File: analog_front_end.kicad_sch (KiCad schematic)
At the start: 14 parts

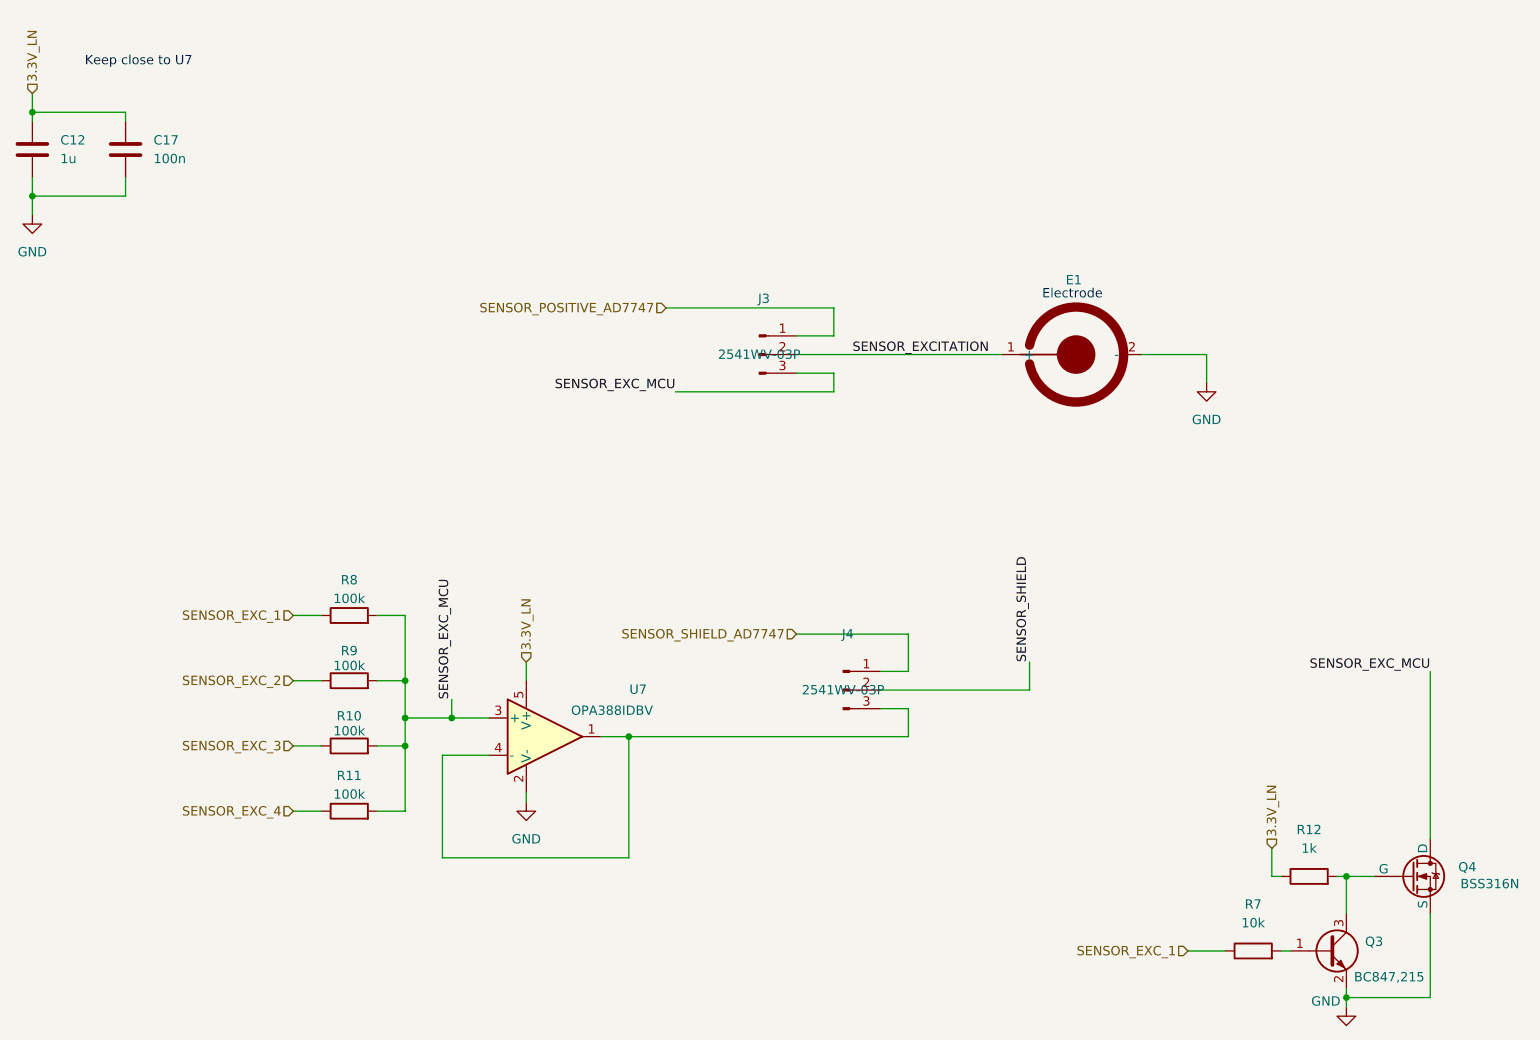
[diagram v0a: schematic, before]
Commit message: bom: Optimize part selection to reduce order price at jlcpcb
- Change references to use basic components instead of 'extended components' when available
- Change button reference to use a basic component
- Change led references to use basic components
- Harmonize some resistors value to limit the number of lines in BoM
- Change transistor references for basic components
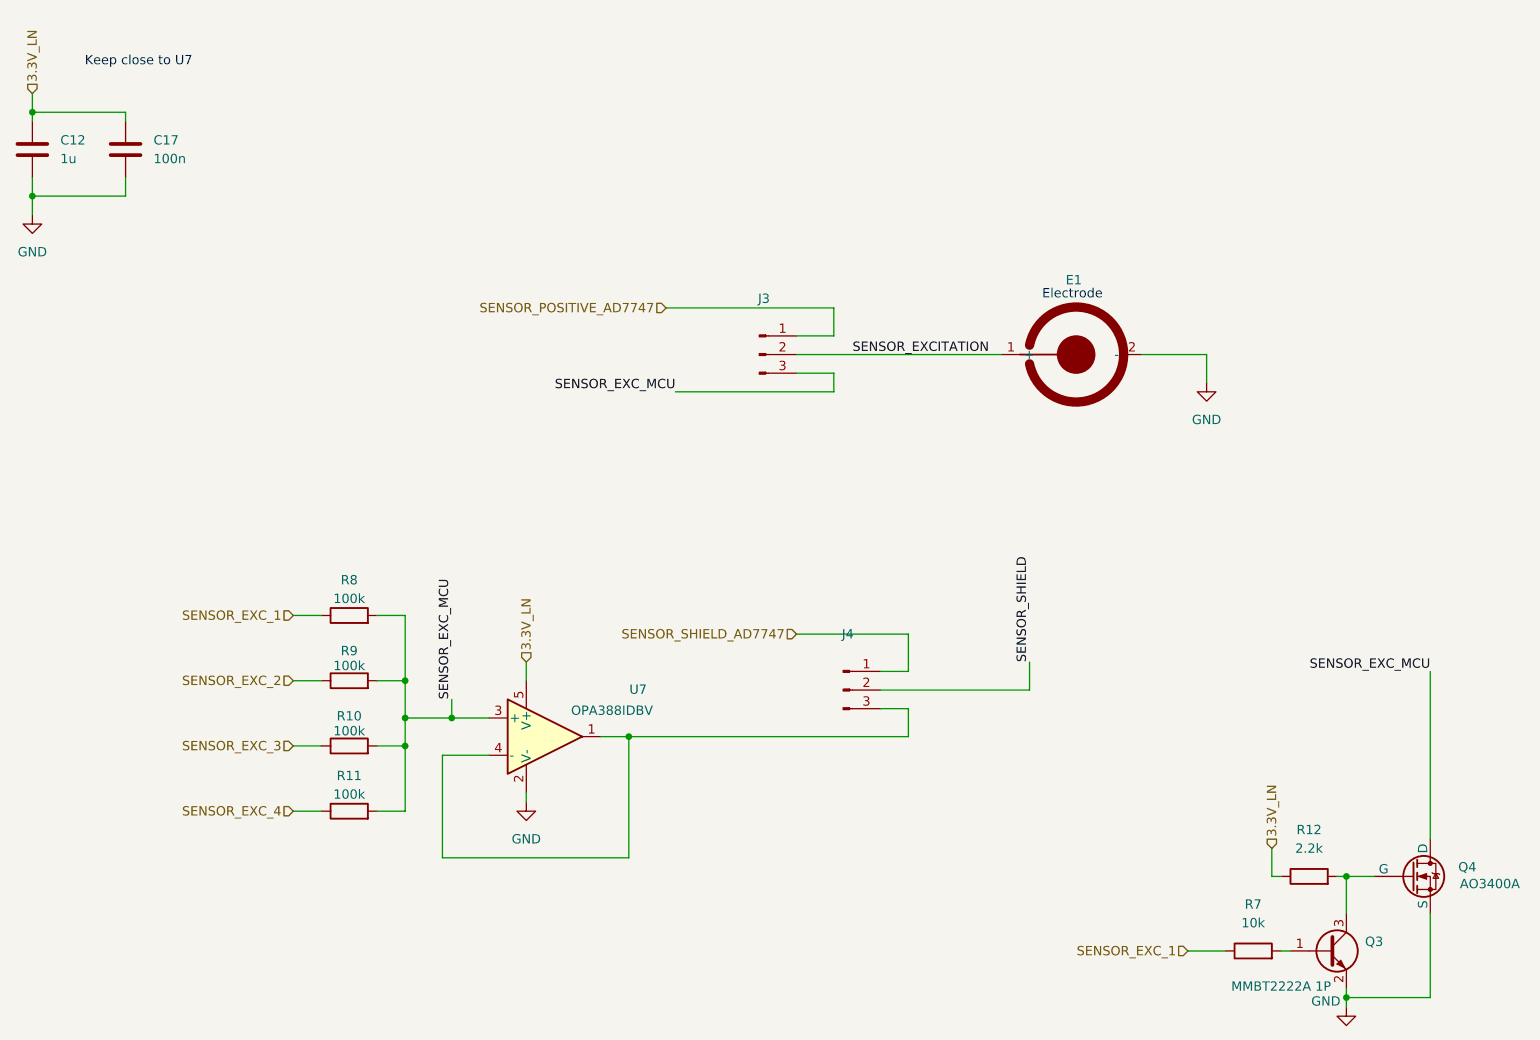
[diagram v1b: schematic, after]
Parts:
- C12: LCSC C59782 -> C15849
- Q3: LCSC C130417 -> C8512; MPN BC847,215 -> MMBT2222A 1P
- Q4: LCSC C19829413 -> C20917; MPN BSS316N -> AO3400A
- R10, R11, R8, R9: LCSC C14675 -> C25803
- R12: value 1k -> 2.2k; LCSC C22548 -> C4190
- R7: LCSC C98220 -> C25804
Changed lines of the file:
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@@
 			)
 		)
-		(property "LCSC" "C98220"
+		(property "LCSC" "C25804"
 			(at 182.88 140.97 0)
 			(effects
@@
 				)
 				(hide yes)
+			)
+		)
+		(property "MPN" ""
+			(at 182.88 140.97 0)
+			(effects
+				(font
+					(size 1.27 1.27)
+				)
 			)
 		)
@@
 			)
 		)
-		(property "LCSC" "C14675"
+		(property "LCSC" "C25803"
 			(at 59.69 113.03 0)
 			(effects
@@
 				)
 				(hide yes)
+			)
+		)
+		(property "MPN" ""
+			(at 59.69 113.03 0)
+			(effects
+				(font
+					(size 1.27 1.27)
+				)
 			)
 		)
@@
 			)
 		)
-		(property "LCSC" "C14675"
+		(property "LCSC" "C25803"
 			(at 59.69 104.14 0)
 			(effects
@@
 				)
 				(hide yes)
+			)
+		)
+		(property "MPN" ""
+			(at 59.69 104.14 0)
+			(effects
+				(font
+					(size 1.27 1.27)
+				)
 			)
 		)
@@
 			)
 		)
-		(property "Value" "1k"
+		(property "Value" "2.2k"
 			(at 190.5 127 90)
 			(effects
@@
 			)
 		)
-		(property "LCSC" "C22548"
+		(property "LCSC" "C4190"
 			(at 190.5 130.81 0)
 			(effects
@@
 				)
 				(hide yes)
+			)
+		)
+		(property "MPN" ""
+			(at 190.5 130.81 0)
+			(effects
+				(font
+					(size 1.27 1.27)
+				)
 			)
 		)
@@
 			)
 		)
-		(property "LCSC" "C19829413"
+		(property "LCSC" "C20917"
 			(at 204.47 130.81 0)
 			(effects
@@
 			)
 		)
-		(property "MPN" "BSS316N"
+		(property "MPN" "AO3400A"
 			(at 215.138 131.826 0)
 			(effects
@@
 		(on_board yes)
 		(dnp no)
-		(fields_autoplaced yes)
 		(property "Reference" "J3"
 			(at 116.205 52.07 0)
@@
 		)
 		(property "MPN" "2541WV-03P"
-			(at 115.57 59.69 0)
-			(effects
-				(font
-					(size 1.27 1.27)
-				)
+			(at 108.458 59.944 0)
+			(effects
+				(font
+					(size 1.27 1.27)
+				)
+				(hide yes)
 			)
 		)
@@
 			)
 		)
-		(property "LCSC" "C130417"
+		(property "LCSC" "C8512"
 			(at 193.04 140.97 0)
 			(effects
@@
 			)
 		)
-		(property "MPN" "BC847,215"
-			(at 201.422 144.526 0)
+		(property "MPN" "MMBT2222A 1P"
+			(at 186.69 145.796 0)
 			(effects
 				(font
@@
 		(on_board yes)
 		(dnp no)
-		(fields_autoplaced yes)
 		(property "Reference" "J4"
 			(at 127.635 97.79 0)
@@
 		)
 		(property "MPN" "2541WV-03P"
-			(at 127 105.41 0)
-			(effects
-				(font
-					(size 1.27 1.27)
-				)
+			(at 119.38 105.664 0)
+			(effects
+				(font
+					(size 1.27 1.27)
+				)
+				(hide yes)
 			)
 		)
@@
 			)
 		)
-		(property "LCSC" "C14675"
+		(property "LCSC" "C25803"
 			(at 59.69 95.25 0)
 			(effects
@@
 				)
 				(hide yes)
+			)
+		)
+		(property "MPN" ""
+			(at 59.69 95.25 0)
+			(effects
+				(font
+					(size 1.27 1.27)
+				)
 			)
 		)
@@
 			)
 		)
-		(property "LCSC" "C14675"
+		(property "LCSC" "C25803"
 			(at 59.69 121.92 0)
 			(effects
@@
 				)
 				(hide yes)
+			)
+		)
+		(property "MPN" ""
+			(at 59.69 121.92 0)
+			(effects
+				(font
+					(size 1.27 1.27)
+				)
 			)
 		)
@@
 			)
 		)
-		(property "LCSC" "C59782"
+		(property "LCSC" "C15849"
 			(at 16.51 31.75 0)
 			(effects
@@
 			)
 		)
+		(property "MPN" ""
+			(at 16.51 31.75 0)
+			(effects
+				(font
+					(size 1.27 1.27)
+				)
+			)
+		)
